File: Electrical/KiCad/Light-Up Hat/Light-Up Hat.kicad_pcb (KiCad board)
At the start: 2 copper layers, 39.9 x 20.1 mm, 18 parts, among them J1 Conn_01x04, Q1 2N3906, SW1 SW_SPST, U1 AP1117-33, U2 PIC10F220-IOT

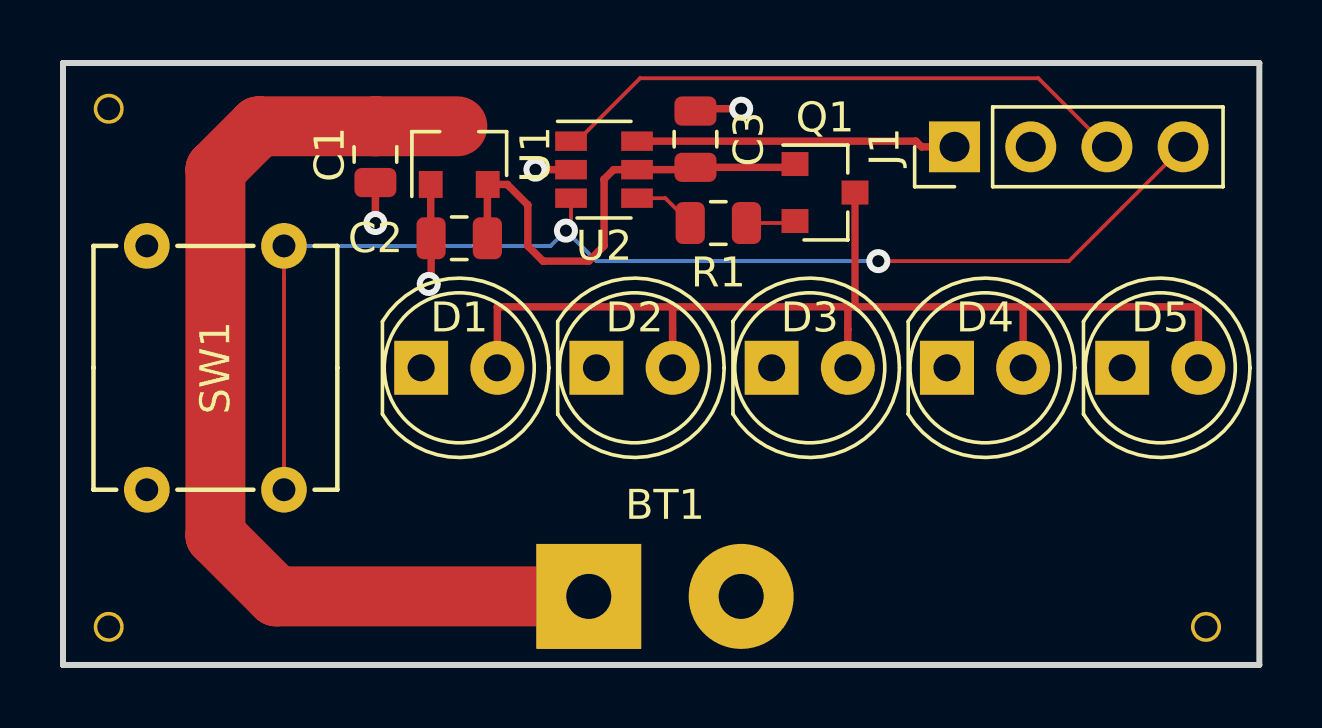
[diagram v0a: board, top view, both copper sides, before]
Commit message: Hat LEDs blink on and off every 1 second
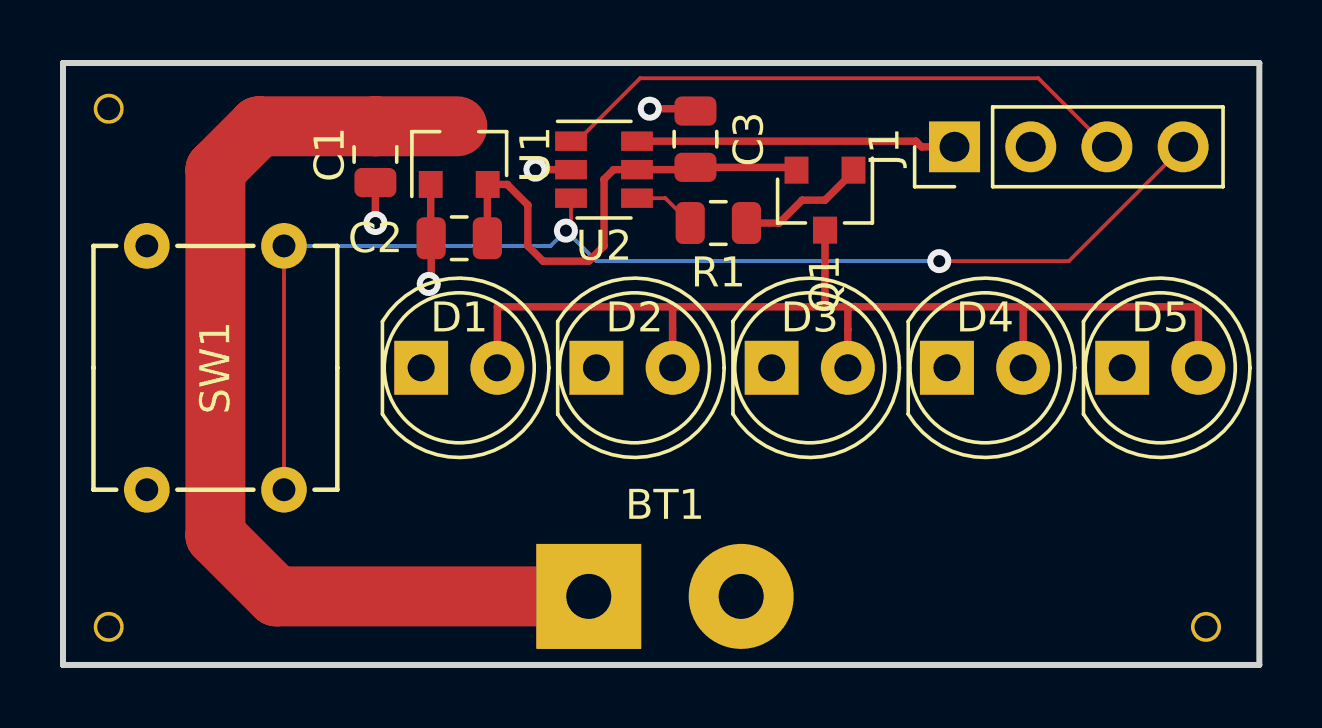
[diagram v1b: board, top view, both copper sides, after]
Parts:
- Q1: value 2N3906 -> MMBT3906
- R1: value 10KΩ -> 1KΩ
- moved Q1 0.25 mm to (149.9, 96.0), turned to 270 degrees
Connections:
- Q1 pad 1: +3V3 -> Net-(Q1-Pad1)
- Q1 pad 2: Net-(Q1-Pad2) -> +3V3
- R1 pad 1: Net-(Q1-Pad2) -> Net-(Q1-Pad1)
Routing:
- net Net-(Q1-Pad1): track 0.00 -> 4.33 mm
- net Net-(Q1-Pad2): track 1.65 -> 0.00 mm
- net Net-(D1-Pad2): track 37.3 -> 36.1 mm
- net GND: track 7.45 -> 8.03 mm

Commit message: fixed board design for new revision
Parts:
- U1: value AP1117-33 -> XC6206
- U2: value PIC10F220-IOT -> PIC10F200-IOT
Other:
- board text added: "+"
- board text added: "-"
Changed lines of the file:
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@@
   (general
     (thickness 1.6)
-    (drawings 6)
+    (drawings 8)
     (tracks 83)
     (zones 0)
@@
       (creategerberjobfile false)
       (excludeedgelayer false)
-      (linewidth 0.100000)
+      (linewidth 0.150000)
       (plotframeref false)
       (viasonmask false)
@@
     (descr "Through hole straight pin header, 1x04, 2.54mm pitch, single row")
     (tags "Through hole pin header THT 1x04 2.54mm single row")
-    (fp_text reference J1 (at 0 -2.33 90) (layer F.SilkS)
+    (fp_text reference J1 (at 1.778 0 180) (layer F.SilkS)
       (effects (font (size 1 1) (thickness 0.15)))
     )
@@
       (effects (font (size 1 1) (thickness 0.15)))
     )
-    (fp_text value PIC10F220-IOT (at 0 2.9) (layer F.Fab)
+    (fp_text value PIC10F200-IOT (at 0 2.9) (layer F.Fab)
       (effects (font (size 1 1) (thickness 0.15)))
     )
@@
     (tags SOT-23)
     (attr smd)
-    (fp_text reference Q1 (at 2.794 0 270) (layer F.SilkS)
+    (fp_text reference Q1 (at -2.54 0) (layer F.SilkS)
       (effects (font (size 1 1) (thickness 0.15)))
     )
@@
     (tags SOT-23)
     (attr smd)
-    (fp_text reference U1 (at 0 2.54 90) (layer F.SilkS)
-      (effects (font (size 1 1) (thickness 0.15)))
-    )
-    (fp_text value AP1117-33 (at 0 2.5 90) (layer F.Fab)
+    (fp_text reference U1 (at 1.524 2.032 180) (layer F.SilkS)
+      (effects (font (size 1 1) (thickness 0.15)))
+    )
+    (fp_text value XC6206 (at 0 2.5 90) (layer F.Fab)
       (effects (font (size 1 1) (thickness 0.15)))
     )
@@
     )
     (pad "" np_thru_hole circle (at 0 0) (size 1 1) (drill 0.762) (layers *.Cu *.Mask))
+  )
+  (gr_text - (at 147.066 106.172) (layer F.SilkS)
+    (effects (font (size 1.5 1.5) (thickness 0.3)))
+  )
+  (gr_text + (at 141.986 106.172) (layer F.SilkS)
+    (effects (font (size 1.5 1.5) (thickness 0.3)))
   )
   (gr_text "EN-HAT-CED PCB\nREV 1.0" (at 143.5862 104.9782) (layer B.SilkS)
@@
   (segment (start 141.224 97.028) (end 142.24 98.044) (width 0.127) (layer B.Cu) (net 6))
   (segment (start 142.24 98.044) (end 150.114 98.044) (width 0.127) (layer B.Cu) (net 6))
+  (segment (start 150.114 98.044) (end 150.114 98.044) (width 0.127) (layer B.Cu) (net 6))
+  (via (at 153.67 98.044) (size 0.8) (drill 0.4) (layers F.Cu B.Cu) (net 6))
+  (segment (start 150.114 98.044) (end 153.67 98.044) (width 0.127) (layer B.Cu) (net 6))
+  (segment (start 157.988 98.044) (end 153.67 98.044) (width 0.127) (layer F.Cu) (net 6))
+  (segment (start 161.798 94.234) (end 157.988 98.044) (width 0.127) (layer F.Cu) (net 6))
+  (segment (start 144.5385 95.946) (end 143.594 95.946) (width 0.127) (layer F.Cu) (net 7))
+  (segment (start 145.3665 96.774) (end 144.5385 95.946) (width 0.127) (layer F.Cu) (net 7))
   (segment (start 156.464 99.568) (end 156.464 101.6) (width 0.25) (layer F.Cu) (net 8))
   (segment (start 138.938 101.6) (end 138.938 99.568) (width 0.25) (layer F.Cu) (net 8))
@@
   (segment (start 150.86 99.552) (end 150.876 99.568) (width 0.25) (layer F.Cu) (net 8))
   (segment (start 150.622 99.568) (end 150.876 99.568) (width 0.25) (layer F.Cu) (net 8))
-  (segment (start 150.114 98.044) (end 150.114 98.044) (width 0.127) (layer B.Cu) (net 6))
-  (via (at 153.67 98.044) (size 0.8) (drill 0.4) (layers F.Cu B.Cu) (net 6))
-  (segment (start 150.114 98.044) (end 153.67 98.044) (width 0.127) (layer B.Cu) (net 6))
-  (segment (start 157.988 98.044) (end 153.67 98.044) (width 0.127) (layer F.Cu) (net 6))
-  (segment (start 161.798 94.234) (end 157.988 98.044) (width 0.127) (layer F.Cu) (net 6))
-  (segment (start 144.5385 95.946) (end 143.594 95.946) (width 0.127) (layer F.Cu) (net 7))
-  (segment (start 145.3665 96.774) (end 144.5385 95.946) (width 0.127) (layer F.Cu) (net 7))
   (segment (start 144.78 99.568) (end 147.828 99.568) (width 0.25) (layer F.Cu) (net 8))
   (segment (start 147.828 99.568) (end 148.59 99.568) (width 0.25) (layer F.Cu) (net 8))
